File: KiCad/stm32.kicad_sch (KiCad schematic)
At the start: 21 parts, among them J15 Conn_01x04, J16 Conn_01x04, J17 Conn_01x04, J18 Conn_01x05, U7 STM32F030C8Tx, Y1 25MHz

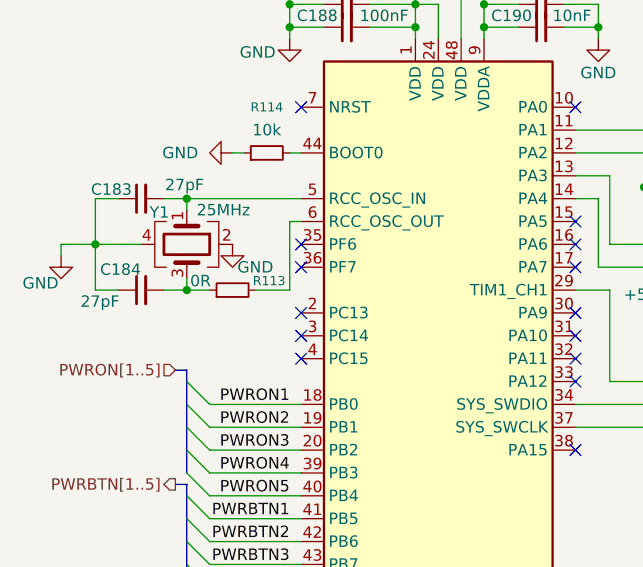
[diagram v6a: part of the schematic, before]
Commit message: Fix esd diodes, add some footprints.
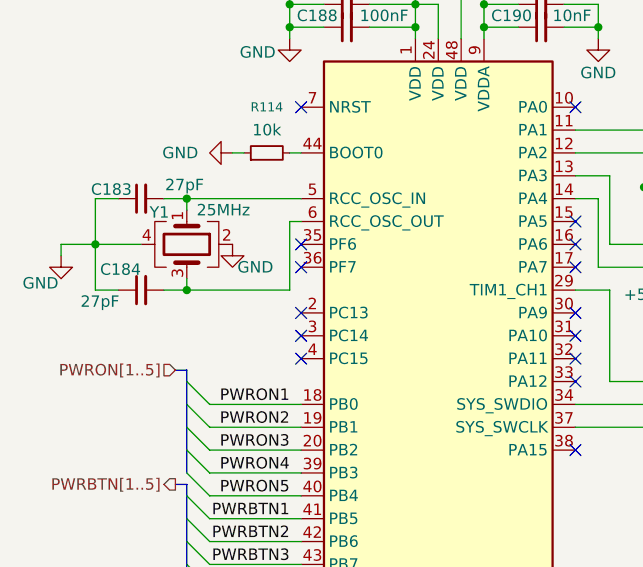
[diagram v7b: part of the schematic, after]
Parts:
- removed R113: 0R, symbol Device:R_Small
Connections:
- net at C184.2, Y1.3: now also U7.6 (PF1)
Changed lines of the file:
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@@
 	(wire
 		(pts
-			(xy 100.33 109.22) (xy 104.14 109.22)
-		)
-		(stroke
-			(width 0)
-			(type default)
-		)
-	)
-	(wire
-		(pts
 			(xy 135.89 91.44) (xy 144.78 91.44)
 		)
@@
 	(wire
 		(pts
-			(xy 92.71 109.22) (xy 95.25 109.22)
+			(xy 92.71 109.22) (xy 104.14 109.22)
 		)
 		(stroke
@@
 					(unit 1)
 				)
-			)
-		)
-	)
-	(symbol
-		(lib_id "Device:R_Small")
-		(at 97.79 109.22 90)
-		(unit 1)
-		(exclude_from_sim no)
-		(in_bom yes)
-		(on_board yes)
-		(dnp no)
-		(property "Reference" "R113"
-			(at 101.854 108.204 90)
-			(effects
-				(font
-					(size 1.016 1.016)
-				)
-			)
-		)
-		(property "Value" "0R"
-			(at 94.234 108.204 90)
-			(effects
-				(font
-					(size 1.27 1.27)
-				)
-			)
-		)
-		(property "Footprint" ""
-			(at 97.79 109.22 0)
-			(effects
-				(font
-					(size 1.27 1.27)
-				)
-				(hide yes)
-			)
-		)
-		(property "Datasheet" "~"
-			(at 97.79 109.22 0)
-			(effects
-				(font
-					(size 1.27 1.27)
-				)
-				(hide yes)
-			)
-		)
-		(property "Description" "Resistor, small symbol"
-			(at 97.79 109.22 0)
-			(effects
-				(font
-					(size 1.27 1.27)
-				)
-				(hide yes)
-			)
-		)
-		(pin "2"
-		)
-		(pin "1"
-		)
-		(instances
-			(project "LattePandaMuCluster"
-				(path "/49abeb3a-c598-45a3-ba6b-595eb04f17a8/6eac886f-f669-4a66-b218-dbac55577930"
-					(reference "R113")
-					(unit 1)
-				)

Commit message: Add more footprints
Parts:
- J15, J16, J17: footprint (none) -> Connector_PinHeader_2.54mm:PinHeader_1x04_P2.54mm_Vertical
- J18: footprint (none) -> Connector_PinHeader_2.54mm:PinHeader_1x05_P2.54mm_Vertical
- Y1: footprint (none) -> Crystal:Crystal_SMD_3225-4Pin_3.2x2.5mm
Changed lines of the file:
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@@
 			)
 		)
-		(property "Footprint" ""
+		(property "Footprint" "Connector_PinHeader_2.54mm:PinHeader_1x04_P2.54mm_Vertical"
 			(at 191.77 88.9 0)
 			(effects
@@
 			)
 		)
-		(property "Footprint" ""
+		(property "Footprint" "Connector_PinHeader_2.54mm:PinHeader_1x04_P2.54mm_Vertical"
 			(at 168.91 116.84 0)
 			(effects
@@
 			)
 		)
-		(property "Footprint" ""
+		(property "Footprint" "Connector_PinHeader_2.54mm:PinHeader_1x05_P2.54mm_Vertical"
 			(at 191.77 102.87 0)
 			(effects
@@
 			)
 		)
-		(property "Footprint" ""
+		(property "Footprint" "Connector_PinHeader_2.54mm:PinHeader_1x04_P2.54mm_Vertical"
 			(at 152.4 114.3 0)
 			(effects
@@
 			)
 		)
-		(property "Footprint" ""
+		(property "Footprint" "Crystal:Crystal_SMD_3225-4Pin_3.2x2.5mm"
 			(at 92.71 104.14 0)
 			(effects
